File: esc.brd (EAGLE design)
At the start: 98.7 x 39.3 mm, 65 parts, among them IC1 78L05F, Q1 16 MHz, T1 IRFR1205, T2 IRFR1205, T3 IRFR1205, T4 IRFR1205, T5 IRFR1205, T6 IRFR1205, U1 ATMEGA48-20AU

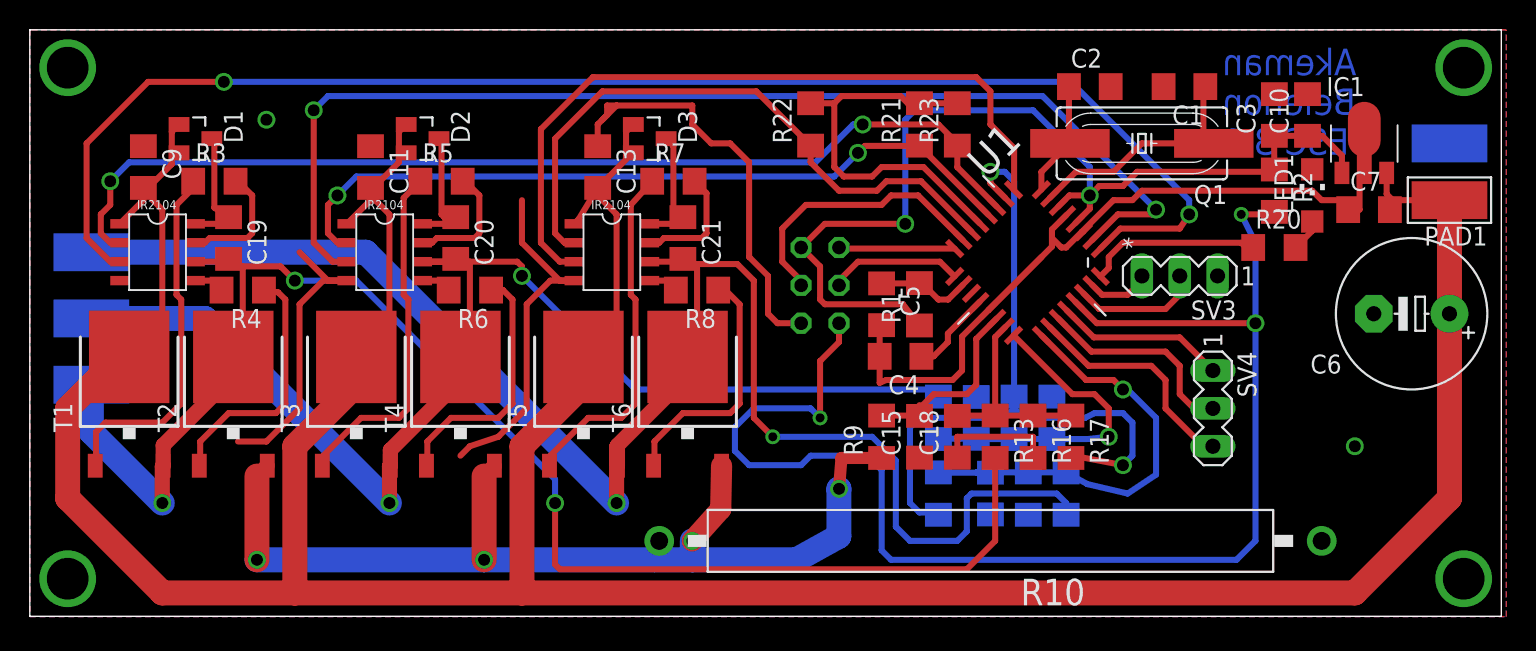
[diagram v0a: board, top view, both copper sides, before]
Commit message: changes for aisler order
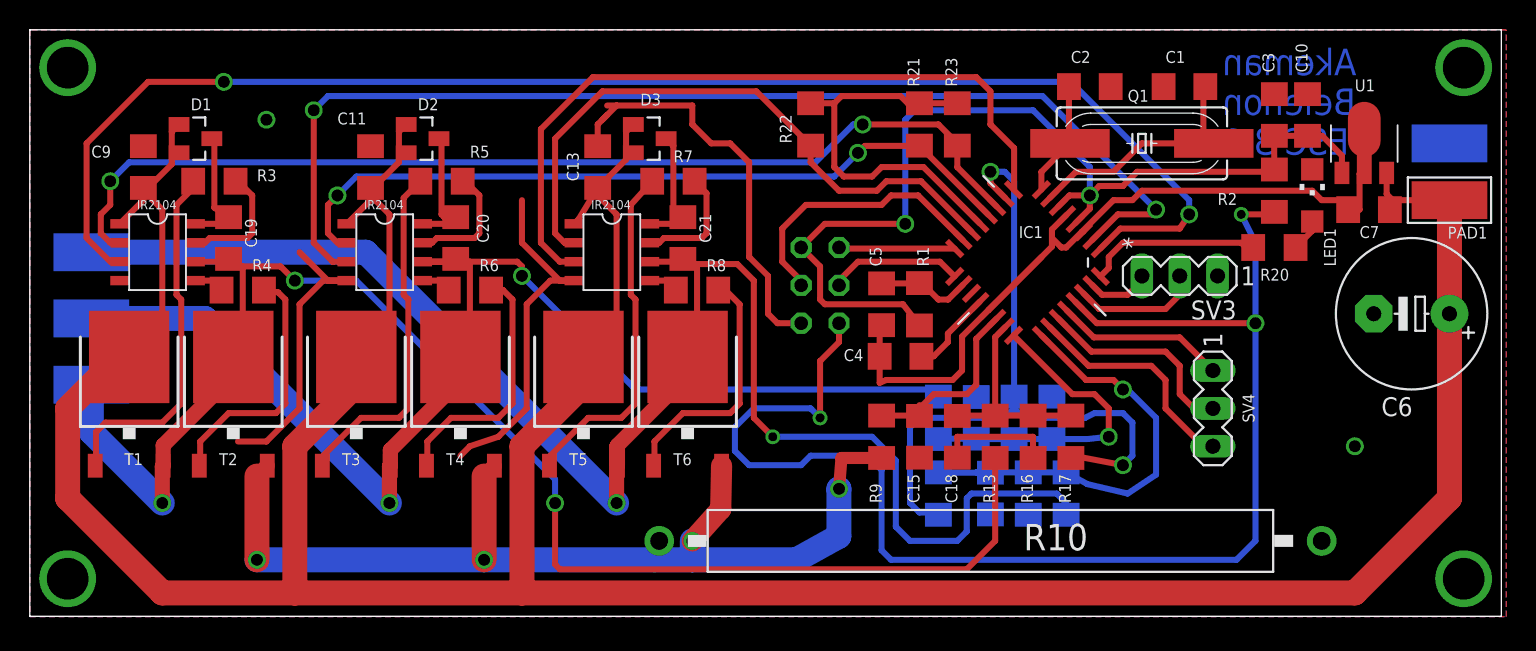
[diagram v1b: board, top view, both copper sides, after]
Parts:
- IC1: value 78L05F -> ATMEGA48-20AU; device linear:SOT89 -> Atmel_By_element14_Batch_1-00:QFP80P900X900X120-32N
- U1: value ATMEGA48-20AU -> 78L05F; device Atmel_By_element14_Batch_1-00:QFP80P900X900X120-32N -> linear:SOT89
- moved IC1 24.0 mm to (66.9, 23.8), turned to 225 degrees
- moved U1 24.0 mm to (89.5, 31.8), turned to 0 degrees
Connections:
- net GND: now also IC1.21, IC1.3, IC1.5, U1.2, U1.2@1; no longer IC1.2, IC1.2@1, U1.21, U1.3, U1.5
- net IN_A: now also IC1.11; no longer U1.11
- net IN_B: now also IC1.12; no longer U1.12
- net IN_C: now also IC1.14; no longer U1.14
- net MISO: now also IC1.16; no longer U1.16
- net MITTEL: now also IC1.10; no longer U1.10
- net MOSI: now also IC1.15; no longer U1.15
- net N$1: now also IC1.7; no longer U1.7
- net N$2: now also IC1.18; no longer U1.18
- net N$24: now also IC1.32; no longer U1.32
- net N$3: now also IC1.8; no longer U1.8
- net N$4: now also IC1.20; no longer U1.20
- net NULL_A: now also IC1.23; no longer U1.23
- net NULL_B: now also IC1.24; no longer U1.24
- net NULL_C: now also IC1.25; no longer U1.25
- net PPM: now also IC1.26; no longer U1.26
- net PWM: now also IC1.13; no longer U1.13
- net RESET: now also IC1.29; no longer U1.29
- net RXD: now also IC1.30; no longer U1.30
- net SCK: now also IC1.17; no longer U1.17
- net SCL: now also IC1.28; no longer U1.28
- net SDA: now also IC1.27; no longer U1.27
- net SD_A: now also IC1.1; no longer U1.1
- net SD_B: now also IC1.2; no longer U1.2
- net SD_C: now also IC1.9; no longer U1.9
- net STROM: now also IC1.22; no longer U1.22
- net TXD: now also IC1.31; no longer U1.31
- net VCC: now also IC1.4, IC1.6, U1.1; no longer IC1.1, U1.4, U1.6
- net VSS: now also U1.3; no longer IC1.3
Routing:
- net GND: track 133.6 -> 133.0 mm

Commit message: aisler
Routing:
- net GND: track 133.0 -> 131.9 mm
- net MITTEL: track 49.4 -> 50.1 mm
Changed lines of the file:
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@@
 <layer number="14" name="Route14" color="1" fill="6" visible="no" active="no"/>
 <layer number="15" name="Route15" color="4" fill="6" visible="no" active="no"/>
-<layer number="16" name="Bottom" color="1" fill="1" visible="no" active="yes"/>
+<layer number="16" name="Bottom" color="1" fill="1" visible="yes" active="yes"/>
 <layer number="17" name="Pads" color="2" fill="1" visible="yes" active="yes"/>
 <layer number="18" name="Vias" color="2" fill="1" visible="yes" active="yes"/>
@@
 <layer number="20" name="Dimension" color="15" fill="1" visible="yes" active="yes"/>
 <layer number="21" name="tPlace" color="7" fill="1" visible="yes" active="yes"/>
-<layer number="22" name="bPlace" color="7" fill="1" visible="no" active="yes"/>
+<layer number="22" name="bPlace" color="7" fill="1" visible="yes" active="yes"/>
 <layer number="23" name="tOrigins" color="15" fill="1" visible="yes" active="yes"/>
-<layer number="24" name="bOrigins" color="15" fill="1" visible="no" active="yes"/>
+<layer number="24" name="bOrigins" color="15" fill="1" visible="yes" active="yes"/>
 <layer number="25" name="tNames" color="7" fill="1" visible="yes" active="yes"/>
-<layer number="26" name="bNames" color="7" fill="1" visible="no" active="yes"/>
+<layer number="26" name="bNames" color="7" fill="1" visible="yes" active="yes"/>
 <layer number="27" name="tValues" color="7" fill="1" visible="no" active="yes"/>
 <layer number="28" name="bValues" color="7" fill="1" visible="no" active="yes"/>
@@
 <layer number="50" name="dxf" color="7" fill="1" visible="no" active="yes"/>
 <layer number="51" name="tDocu" color="7" fill="1" visible="yes" active="yes"/>
-<layer number="52" name="bDocu" color="7" fill="1" visible="no" active="yes"/>
+<layer number="52" name="bDocu" color="7" fill="1" visible="yes" active="yes"/>
 <layer number="91" name="Nets" color="2" fill="1" visible="no" active="no"/>
 <layer number="92" name="Busses" color="1" fill="1" visible="no" active="no"/>
@@
 <wire x1="98.73" y1="0.02" x2="98.73" y2="39.37" width="0" layer="20"/>
 <wire x1="98.73" y1="39.37" x2="0" y2="39.37" width="0" layer="20"/>
-<text x="80.01" y="38.1" size="1.778" layer="16" rot="MR180">Akeman
+<text x="77.1525" y="38.1" size="1.778" layer="16" rot="MR180">Akeman
 Belenon
 ESC 3.1</text>
@@
 <wire x1="62.5475" y1="16.51" x2="61.9125" y2="15.875" width="0.4064" layer="1"/>
 <wire x1="61.9125" y1="15.875" x2="57.4675" y2="15.875" width="0.4064" layer="1"/>
-<wire x1="57.4675" y1="15.875" x2="57.02" y2="15.6875" width="0.4064" layer="1"/>
-<wire x1="57.02" y1="15.6875" x2="57.02" y2="17.4625" width="0.4064" layer="1"/>
+<wire x1="57.4675" y1="15.875" x2="57.02" y2="16.3225" width="0.4064" layer="1"/>
+<wire x1="57.02" y1="16.3225" x2="57.02" y2="17.4625" width="0.4064" layer="1"/>
 <wire x1="18.0975" y1="24.4475" x2="20.0025" y2="22.5425" width="0.4064" layer="1"/>
 <wire x1="20.0025" y1="22.5425" x2="21.2725" y2="22.5425" width="0.4064" layer="1"/>
@@
 <wire x1="57.02" y1="19.3675" x2="57.02" y2="17.4625" width="0.4064" layer="1"/>
 <wire x1="44.45" y1="34.29" x2="39.37" y2="34.29" width="0.4064" layer="1"/>
-<wire x1="39.37" y1="34.29" x2="38.735" y2="34.29" width="0.4064" layer="1"/>
 <wire x1="38.735" y1="33.655" x2="38.4175" y2="33.3375" width="0.4064" layer="1"/>
 <wire x1="70.590984375" y1="25.823484375" x2="72.7075" y2="27.94" width="0.4064" layer="1"/>
@@
 <wire x1="44.45" y1="5.08" x2="44.45" y2="3.81" width="1.6764" layer="16"/>
 <via x="54.2925" y="8.5725" extent="1-16" drill="0.8"/>
-<wire x1="54.2925" y1="8.5725" x2="54.458" y2="10.643" width="0.8128" layer="1"/>
-<wire x1="54.458" y1="10.643" x2="57.15" y2="10.643" width="0.8128" layer="1"/>
+<wire x1="54.2925" y1="8.5725" x2="55.093" y2="10.643" width="0.8128" layer="1"/>
+<wire x1="55.093" y1="10.643" x2="57.15" y2="10.643" width="0.8128" layer="1"/>
 <wire x1="54.2925" y1="8.5725" x2="54.2825" y2="8.5725" width="1.27" layer="16"/>
 <wire x1="42.2275" y1="5.08" x2="41.91" y2="3.81" width="1.27" layer="16"/>
@@
 <via x="64.4525" y="29.845" extent="1-16" drill="0.8"/>
 <wire x1="69.85" y1="10.643" x2="70.002" y2="10.795" width="0.4064" layer="1"/>
-<wire x1="70.002" y1="10.795" x2="73.3425" y2="10.16" width="0.4064" layer="1"/>
+<wire x1="70.002" y1="10.795" x2="69.85" y2="10.16" width="0.4064" layer="1"/>
+<wire x1="69.85" y1="10.16" x2="73.3425" y2="10.16" width="0.4064" layer="1"/>
 <via x="73.3425" y="10.16" extent="1-16" drill="0.8"/>
 <wire x1="73.3425" y1="10.16" x2="73.9775" y2="10.795" width="0.4064" layer="16"/>
